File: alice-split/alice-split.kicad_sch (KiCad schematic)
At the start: 127 parts, among them SW38 SW_PUSH-MX_W_LED, SW39 SW_PUSH-MX_W_LED, SW40 SW_PUSH-MX_W_LED, SW41 SW_PUSH-MX_W_LED, SW42 SW_PUSH-MX_W_LED, SW43 SW_PUSH-MX_W_LED, SW44 SW_PUSH-MX_W_LED, SW45 SW_PUSH-MX_W_LED, SW46 SW_PUSH-MX_W_LED, SW47 SW_PUSH-MX_W_LED, SW48 SW_PUSH-MX_W_LED, SW49 SW_PUSH-MX_W_LED, SW50 SW_PUSH-MX_W_LED, SW51 SW_PUSH-MX_W_LED, SW52 SW_PUSH-MX_W_LED, SW53 SW_PUSH-MX_W_LED, SW54 SW_PUSH-MX_W_LED, SW55 SW_PUSH-MX_W_LED, SW56 SW_PUSH-MX_W_LED, SW57 SW_PUSH-MX_W_LED, SW58 SW_PUSH-MX_W_LED, SW59 SW_PUSH-MX_W_LED, SW60 SW_PUSH-MX_W_LED, SW61 SW_PUSH-MX_W_LED, SW62 SW_PUSH-MX_W_LED, SW63 SW_PUSH-MX_W_LED, SW64 SW_PUSH-MX_W_LED, SW65 SW_PUSH-MX_W_LED, SW66 SW_PUSH-MX_W_LED, SW67 SW_PUSH-MX_W_LED, SW68 SW_PUSH-MX_W_LED, SW69 SW_PUSH-MX_W_LED, SW70 SW_PUSH-MX_W_LED, SW71 SW_PUSH-MX_W_LED, SW72 SW_PUSH-MX_W_LED, SW73 SW_PUSH-MX_W_LED, SW74 SW_PUSH-MX_W_LED, SW75 SW_PUSH-MX_W_LED, SW76 SW_PUSH-MX_W_LED, SW77 SW_PUSH-MX_W_LED, SW78 SW_PUSH-MX_W_LED, SW79 SW_PUSH-MX_W_LED, SW80 SW_PUSH-MX_W_LED, SW81 SW_PUSH-MX_W_LED, SW82 SW_PUSH-MX_W_LED, SW83 SW_PUSH-MX_W_LED, SW84 SW_PUSH-MX_W_LED, SW85 SW_PUSH-MX_W_LED, SW86 SW_PUSH-MX_W_LED, SW87 SW_PUSH-MX_W_LED, SW88 SW_PUSH-MX_W_LED, SW89 SW_PUSH-MX_W_LED

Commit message: Drew curved traces instead of the usual defaults. Not sure I like it. Going to branch and try again.
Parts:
- added U1: Sparkfun_Pro_Micro, Keebio-Parts:ArduinoProMicro, symbol Arduino:Sparkfun_Pro_Micro
- SW38, SW41, SW42, SW43, SW44, SW45, SW46, SW47, SW48, SW49, SW50, SW51, SW52, SW53, SW54, SW55, SW56, SW57, SW58, SW59, SW60, SW61, SW62, SW63, SW64, SW65, SW66, SW67, SW68, SW69, SW70, SW71, SW72, SW73, SW74, SW75, SW76, SW77, SW78, SW79, SW80, SW81, SW82, SW83, SW84, SW85, SW86, SW87, SW88, SW89, SW_1, SW_2, SW_3, SW_4, SW_5, SW_6, SW_A1, SW_B_L1, SW_C1, SW_CTRL_L1, SW_D1, SW_E1, SW_ESC1, SW_F1, SW_F2, SW_F3, SW_F4, SW_F5, SW_F6, SW_F7, SW_F8, SW_FN1, SW_G1, SW_MOD_L1, SW_OPT1, SW_Q1, SW_R1, SW_S1, SW_SPC_L1, SW_T1, SW_TILDE1, SW_V1, SW_W1, SW_X1, SW_Z1: footprint Button_Switch_Keyboard:SK6812MINI_and_cherry -> SofleRGB:SK6812MINI_and_cherry
- SW_CAPS1, SW_SHIFT_L1, SW_TAB1: footprint SofleKeyboard-footprint:CherryMX_Hotswap_1.5 -> SofleRGB:SK6812MINI_and_cherry
- SW_M1: renamed from SW40; footprint Button_Switch_Keyboard:SK6812MINI_and_cherry -> SofleRGB:SK6812MINI_and_cherry
- SW_M2: renamed from SW39; footprint Button_Switch_Keyboard:SK6812MINI_and_cherry -> SofleRGB:SK6812MINI_and_cherry
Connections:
- net COL10: now also U1.18 (D19/A1); no longer D11.2 (A), D18.2 (A), D24.2 (A), D30.2 (A), D35.2 (A), D4.2 (A), SW_3.5, SW_C1.5, SW_D1.5, SW_E1.5, SW_F3.5, SW_MOD_L1.5
- net COL11: now also U1.17 (D18/A0); no longer D12.2 (A), D17.2 (A), D23.2 (A), D29.2 (A), D3.2 (A), D34.2 (A), SW_2.5, SW_F2.5, SW_OPT1.5, SW_S1.5, SW_W1.5, SW_X1.5
- net COL12: now also U1.16 (D15); no longer D13.2 (A), D16.2 (A), D2.2 (A), D22.2 (A), D28.2 (A), SW_1.5, SW_A1.5, SW_F1.5, SW_Q1.5, SW_Z1.5
- net COL13: now also U1.15 (D14); no longer D1.2 (A), D14.2 (A), D15.2 (A), D21.2 (A), D27.2 (A), D33.2 (A), SW_CAPS1.5, SW_CTRL_L1.5, SW_ESC1.5, SW_SHIFT_L1.5, SW_TAB1.5, SW_TILDE1.5
- net COL14: now also U1.14 (D16); no longer SW_ESC1.6
- net COL8: now also U1.20 (D21/A3); no longer D6.2 (A), D9.2 (A), SW_5.5, SW_F5.5
- net COL9: now also U1.19 (D20/A2); no longer D10.2 (A), D19.2 (A), D25.2 (A), D31.2 (A), D36.2 (A), D5.2 (A), SW_4.5, SW_F4.5, SW_F8.5, SW_R1.5, SW_SPC_L1.5, SW_V1.5
- net GND: now also U1.23 (GND)
- net LEDs: now also U1.1 (D1/TX)
- net ROW0: now also U1.6 (~D3)
- net ROW1: now also U1.7 (D4/A6)
- net ROW2: now also U1.8 (~D5)
- net ROW3: now also U1.9 (~D6/A7)
- net ROW4: now also U1.10 (D7)
- net ROW5: now also U1.11 (D8/A8)
- net VCC: now also U1.21 (VCC)
- new net: D25.2 (A), SW_F8.5
- new net: D3.2 (A), SW_F2.5
- new net: D1.2 (A), SW_ESC1.5
- new net: D36.2 (A), SW_SPC_L1.5
- new net: D34.2 (A), SW_OPT1.5
- new net: D28.2 (A), SW_Z1.5
- new net: D30.2 (A), SW_C1.5
- new net: D35.2 (A), SW_MOD_L1.5
- new net: D15.2 (A), SW_TAB1.5
- new net: D11.2 (A), SW_3.5
- new net: D4.2 (A), SW_F3.5
- new net: D21.2 (A), SW_CAPS1.5
- new net: D6.2 (A), SW_F5.5
- new net: D9.2 (A), SW_5.5
- new net: D33.2 (A), SW_CTRL_L1.5
- new net: D22.2 (A), SW_A1.5
- new net: D19.2 (A), SW_R1.5
- new net: D17.2 (A), SW_W1.5
- new net: D23.2 (A), SW_S1.5
- new net: D27.2 (A), SW_SHIFT_L1.5
- new net: D18.2 (A), SW_E1.5
- new net: D31.2 (A), SW_V1.5
- new net: D16.2 (A), SW_Q1.5
- new net: D10.2 (A), SW_4.5
- new net: D24.2 (A), SW_D1.5
- new net: D13.2 (A), SW_1.5
- new net: D2.2 (A), SW_F1.5
- new net: D14.2 (A), SW_TILDE1.5
- new net: D5.2 (A), SW_F4.5
- new net: D12.2 (A), SW_2.5
- new net: D29.2 (A), SW_X1.5
- new net COL15: SW_ESC1.6, U1.13 (~D10/A10)
- new net ROW6: U1.12 (~D9/A9)
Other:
- moved on the sheet: D1, D10, D11, D12, D13, D14, D15, D16, D17, D18, D19, D2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

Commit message: Redid the traces but with the usual 45 degree traces. Looks nicer, made more progress.
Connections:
- net COL10: no longer SW_F4.6
- net COL11: no longer SW_F3.6
- net COL12: no longer SW_F2.6
- net COL13: no longer SW_F1.6
- net COL14: now also SW_ESC1.6; no longer SW_TILDE1.6
- net COL15: no longer SW_ESC1.6, U1.13 (~D10/A10)
- net COL8: no longer SW_F6.6
- net COL9: no longer SW_F5.6
- net GND: now also SW_E1.4 (VDD), SW_Q1.4 (VDD), SW_R1.4 (VDD), SW_TAB1.4 (VDD), SW_W1.4 (VDD), U1.3 (GND), U1.4 (GND); no longer SW_F1.4 (VDD), SW_F2.4 (VDD), SW_F3.4 (VDD), SW_F4.4 (VDD), SW_F5.4 (VDD), SW_F6.4 (VDD), SW_TILDE1.4 (VDD), U1.23 (GND)
- net ROW0: now also U1.5 (D2); no longer U1.6 (~D3)
- net ROW1: now also U1.6 (~D3); no longer U1.7 (D4/A6)
- net ROW2: now also U1.7 (D4/A6); no longer U1.8 (~D5)
- net ROW3: now also U1.8 (~D5); no longer U1.9 (~D6/A7)
- net ROW4: now also D1.1 (K), U1.9 (~D6/A7); no longer D14.1 (K), U1.10 (D7)
- net ROW5: no longer D1.1 (K), D2.1 (K), D3.1 (K), D4.1 (K), D5.1 (K), D6.1 (K), D7.1 (K), U1.11 (D8/A8)
- net VCC: no longer SW_F1.2 (VSS), SW_F2.2 (VSS), SW_F3.2 (VSS), SW_F4.2 (VSS), SW_F5.2 (VSS), SW_F6.2 (VSS), SW_TILDE1.2 (VSS)
- net at SW_1.1 (DOUT): now also SW_ESC1.3 (DIN); no longer SW_TILDE1.3 (DIN)
- net at SW_TILDE1.1 (DOUT): no longer SW_F6.3 (DIN)
- net at SW_F1.1 (DOUT): no longer SW_ESC1.3 (DIN)
- net at D14.2 (A): no longer SW_TILDE1.5
- net ROW6: no longer names the net of U1.12 (~D9/A9)
- new net: SW_6.3 (DIN), SW_TAB1.1 (DOUT)
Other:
- moved on the sheet: D1, D14, D2, D3, D4, D5, D6, D7, SW_ESC1A, SW_F1A, SW_F1B, SW_F2A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

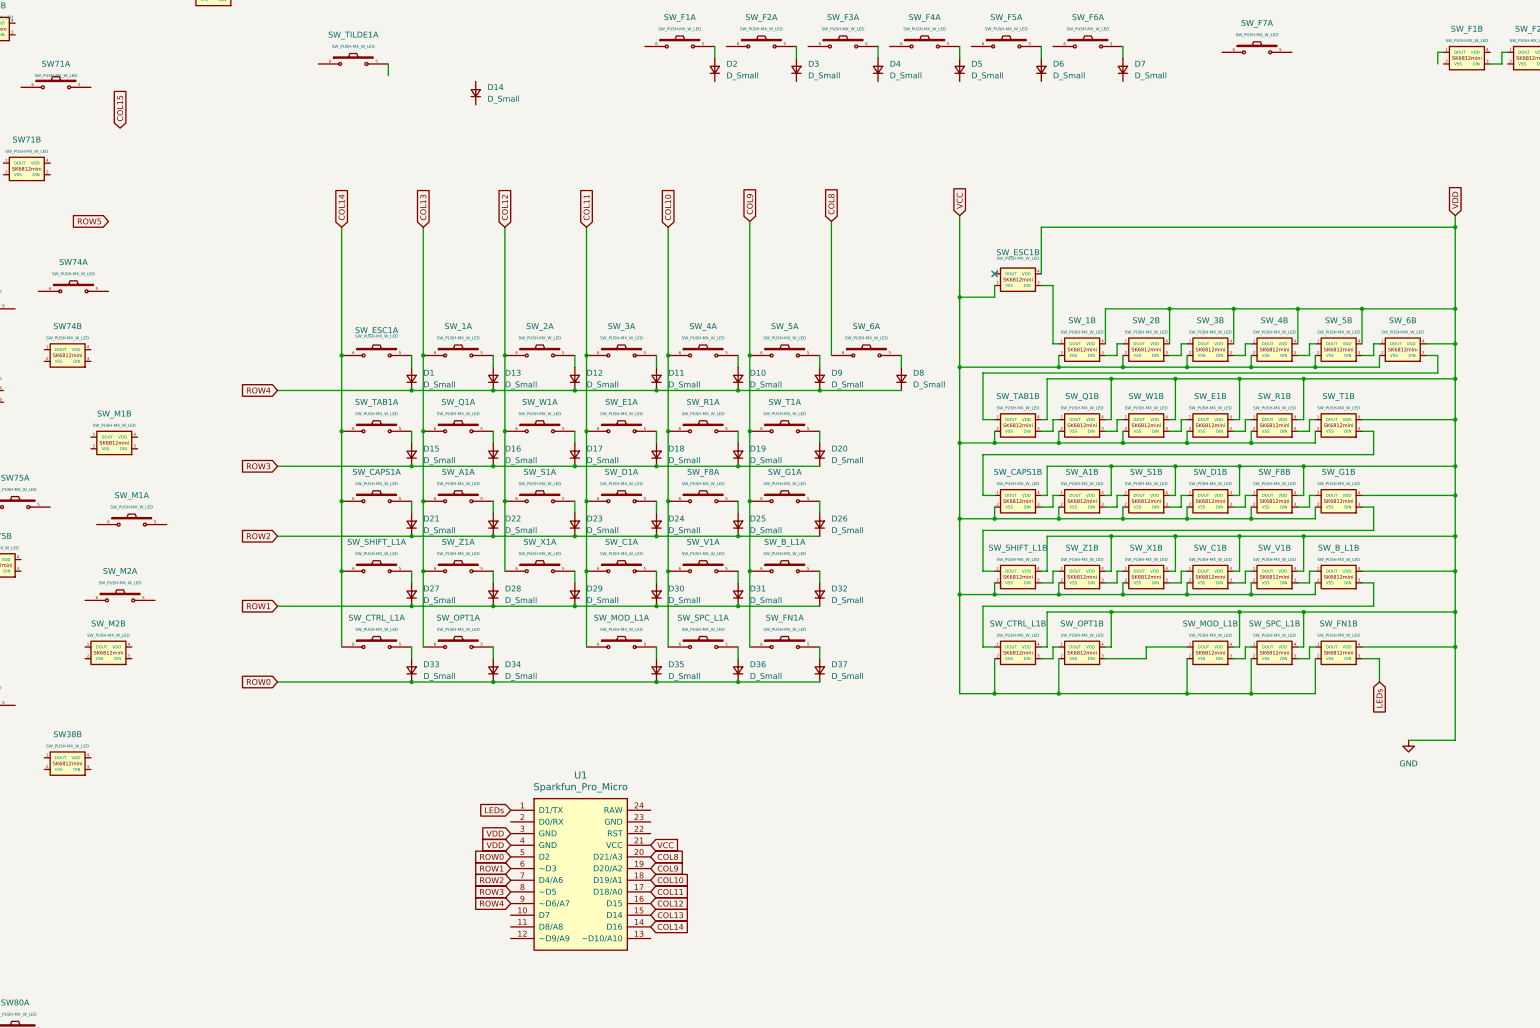
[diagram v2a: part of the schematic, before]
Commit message: Added encoder and macro keys. Whole lefthand side is wired. Needs another review.
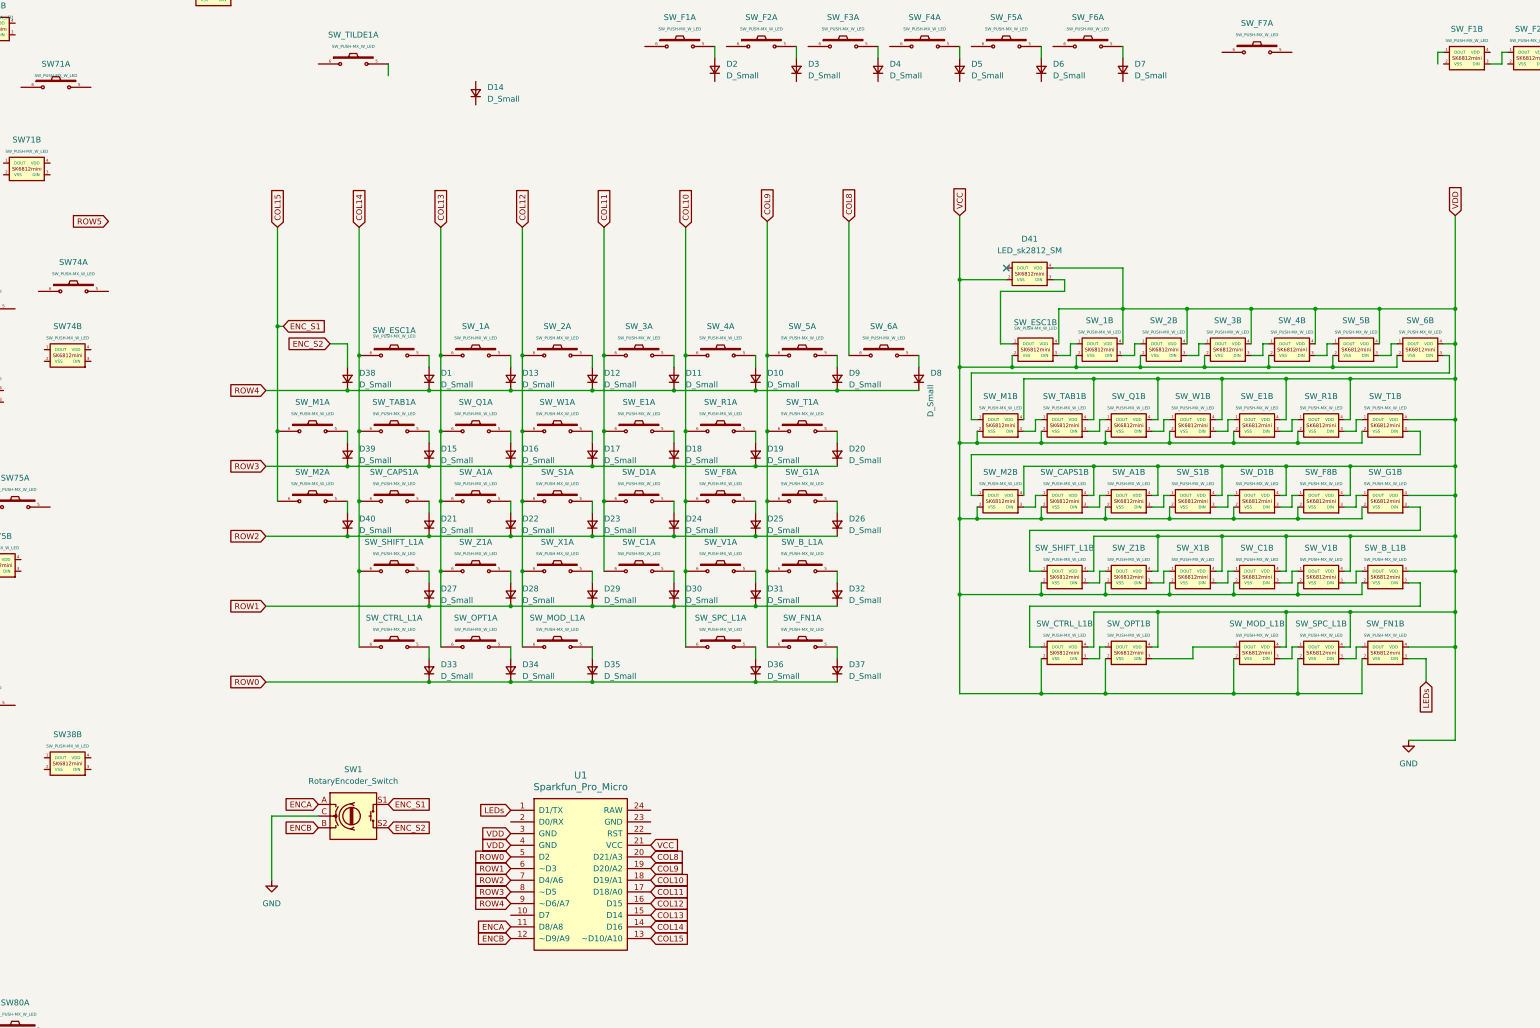
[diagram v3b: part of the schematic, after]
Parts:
- added D38, D39, D40: D_Small, Diode_SMD:D_1206_3216Metric, symbol Device:D_Small
- added D41: LED_sk2812_SM, SofleRGB:SK6812MINI_underglow_dev, symbol SofleKeyboard:LED_sk2812_SM
- added SW1: RotaryEncoder_Switch, SofleRGB:RotaryEncoder_Alps_EC11E-Switch_Vertical_H20mm-keebio_modified, symbol Device:RotaryEncoder_Switch
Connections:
- net COL11: no longer SW_MOD_L1.6
- net COL12: now also SW_MOD_L1.6
- net COL15: now also SW_M1.6, SW_M2.6, U1.13 (~D10/A10), SW1.S1
- net GND: now also SW_M1.4 (VDD), SW_M2.4 (VDD), D41.4 (VDD), SW1.C
- net ROW2: now also D40.1 (K)
- net ROW3: now also D39.1 (K)
- net ROW4: now also D38.1 (K)
- net VCC: now also SW_M1.2 (VSS), SW_M2.2 (VSS), D41.2 (VSS)
- net at SW_M1.5: now also D39.2 (A)
- net at SW_M1.1 (DOUT): now also SW_6.3 (DIN)
- net at SW_M1.3 (DIN): now also SW_TAB1.1 (DOUT)
- net at SW_CAPS1.1 (DOUT): now also SW_M2.3 (DIN); no longer SW_T1.3 (DIN)
- net at SW_M2.5: now also D40.2 (A)
- net ENCA: now reaches U1.11 (D8/A8)
- net ENCA: now also SW1.A
- net ENCB: now reaches U1.12 (~D9/A9)
- net ENCB: now also SW1.B
- net at SW_M2.1 (DOUT): now also SW_T1.3 (DIN)
- net at SW_ESC1.1 (DOUT): now also D41.3 (DIN)
- new net ENC_S2: D38.2 (A), SW1.S2
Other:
- moved on the sheet: D1, D10, D11, D12, D13, D15, D16, D17, D18, D19, D20, D21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

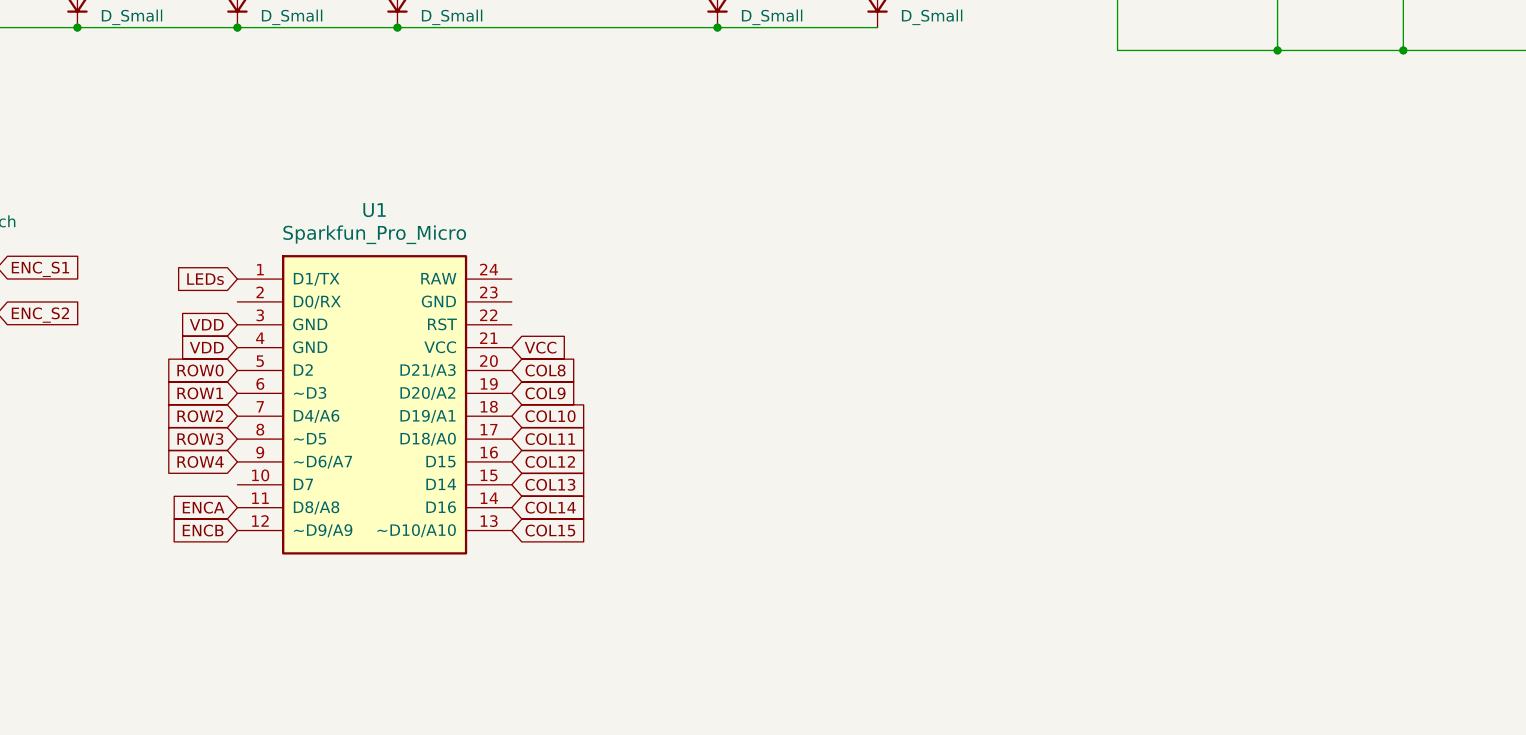
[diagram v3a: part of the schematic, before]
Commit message: Updating repo after adding the backups to the gitignore file.
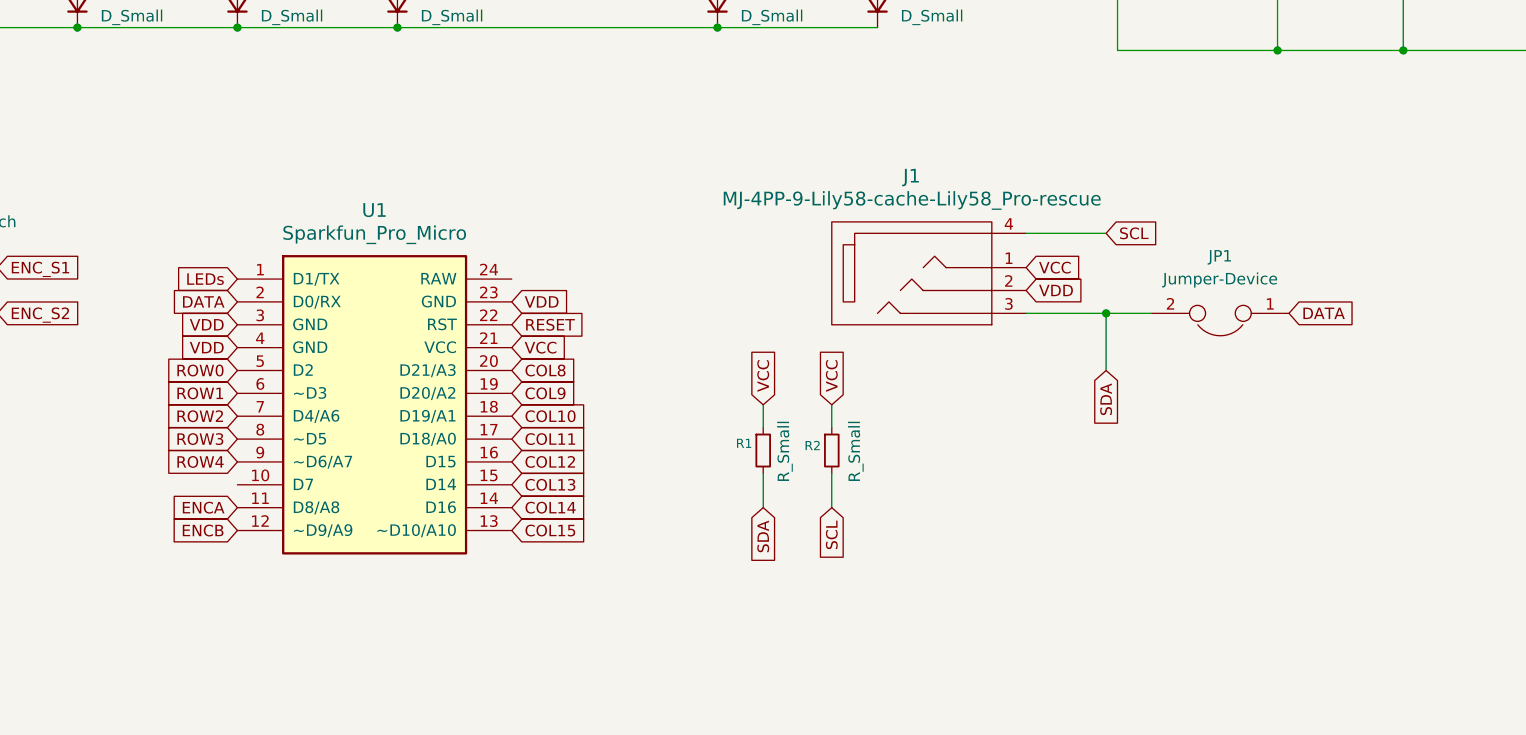
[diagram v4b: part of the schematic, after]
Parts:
- added J1: MJ-4PP-9-Lily58-cache-Lily58_Pro-rescue, SofleRGB:MJ-4PP-9, symbol SofleKeyboard-rescue:MJ-4PP-9-Lily58-cache-Lily58_Pro-rescue
- added JP1: Jumper-Device, SofleRGB:jumper_data, symbol SofleKeyboard-rescue:Jumper-Device
- added R1, R2: R_Small, SofleKeyboard-footprint:R_1206_DoubleSided, symbol Device:R_Small
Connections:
- net GND: now also U1.23 (GND), J1.2
- net VCC: now also J1.1, R1.1, R2.1
- net DATA: now reaches U1.2 (D0/RX)
- net DATA: now also JP1.1
- net RESET: now reaches U1.22 (RST)
- new net SCL: J1.4, R2.2
- new net SDA: J1.3, JP1.2, R1.2
